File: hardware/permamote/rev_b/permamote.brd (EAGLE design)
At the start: 27 x 60 mm, 125 parts, among them J1 TC2030-JLINK-NL, J5 MICRO_USB_B_HIROSE_ZX62R-B-5P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, Q1 PMDXB950UPEL, Q10 PMDXB950UPEL, Q2 PMDXB950UPEL, Q3 PMDXB950UPEL, Q4 PMDXB950UPEL, Q5 PMDXB950UPEL, Q6 PMDXB950UPEL, Q7 PMDXB950UPEL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

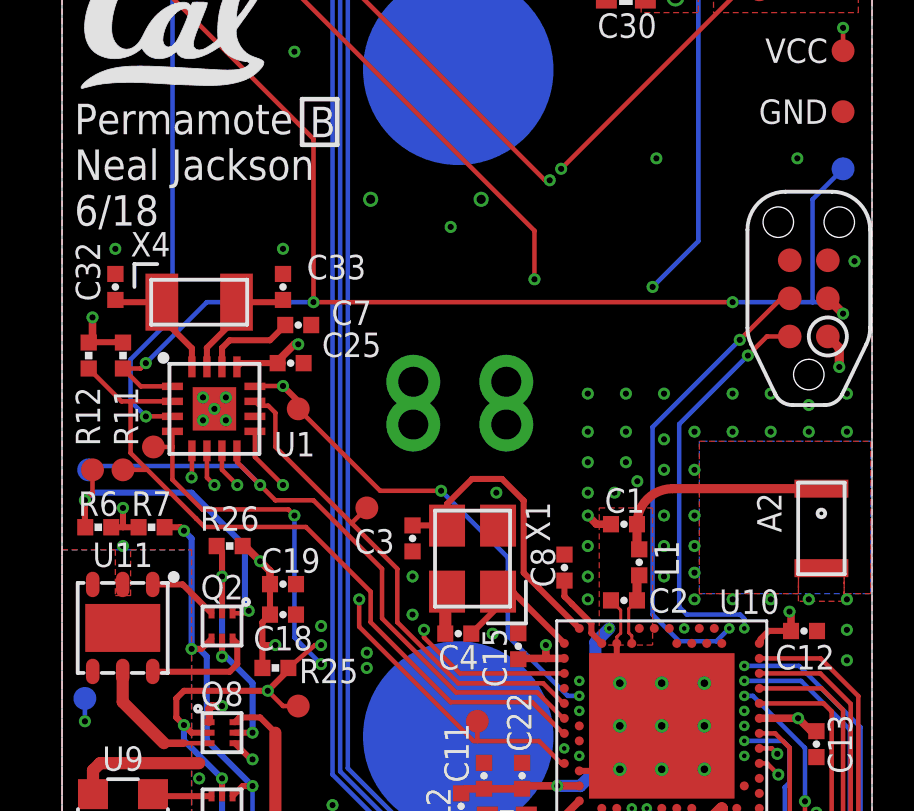
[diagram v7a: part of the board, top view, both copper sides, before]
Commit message: Update to nrf52840 v1.0 spec
Add decoupling cap to DEC5
Change values of RF passives
mentioned in #3
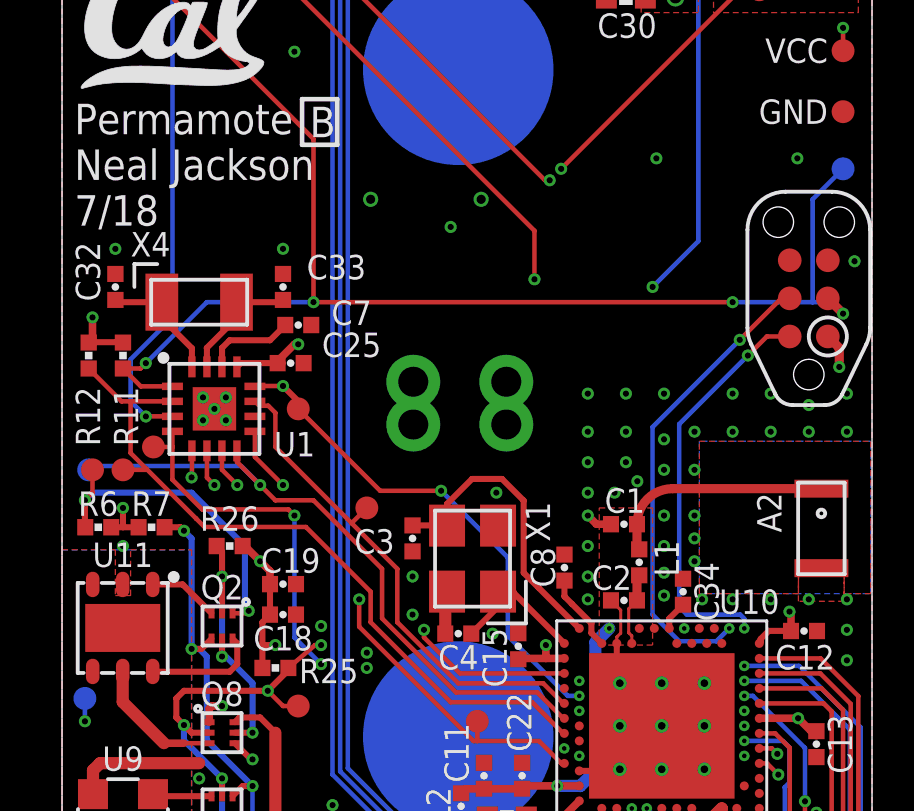
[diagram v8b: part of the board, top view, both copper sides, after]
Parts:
- added C34: 820pF, passives:0402_CAP
- C1: value 0.5pF -> 1pF
- C2: value 0.8pF -> 1pF
- L1: value 3.3nH -> 3.9nH
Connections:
- new net N$1: C34.1, U10.N24
- net GND: now also C34.2
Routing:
- net N$1: track 0.00 -> 0.98 mm
- net GND: vias 109 -> 110
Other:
- board text added: "Permamote Neal Jackson 7/18"
- board text removed: "Permamote Neal Jackson 6/18"
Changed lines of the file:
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@@
 <?xml version="1.0" encoding="utf-8"?>
 <!DOCTYPE eagle SYSTEM "eagle.dtd">
-<eagle version="9.0.0">
+<eagle version="9.0.1">
 <drawing>
 <settings>
@@
 <text x="0.413" y="37.349" size="1.016" layer="25" font="vector" ratio="12" align="top-left">Permamote
 Neal Jackson
-6/18</text>
+7/18</text>
 <polygon width="0.1016" layer="41">
 <vertex x="12.446" y="1.7907"/>
@@
 <attribute name="NAME" x="13.208" y="19.304" size="0.8128" layer="25" font="vector" ratio="12" rot="R180" align="bottom-center"/>
 </element>
-<element name="C2" library="passives" package="0402_CAP" value="0.8pF" x="18.732" y="20.793" smashed="yes" rot="R180">
-<attribute name="DIGIKEY" value="490-6269-1-ND" x="18.732" y="20.793" size="1.778" layer="27" rot="R180" display="off"/>
-<attribute name="MPN" value="GRM1555C1HR80BA01D " x="18.732" y="20.793" size="1.778" layer="27" rot="R180" display="off"/>
-<attribute name="NAME" x="20.228" y="20.383" size="0.8128" layer="25" font="vector" ratio="12" align="bottom-center"/>
-</element>
-<element name="C1" library="passives" package="0402_CAP" value="0.5pF" x="18.732" y="23.333" smashed="yes" rot="R180">
-<attribute name="DIGIKEY" value="490-6264-1-ND" x="18.732" y="23.333" size="1.778" layer="27" rot="R180" display="off"/>
-<attribute name="MPN" value="GRM1555C1HR50WA01D " x="18.732" y="23.333" size="1.778" layer="27" rot="R180" display="off"/>
+<element name="C2" library="passives" package="0402_CAP" value="1pF" x="18.732" y="20.793" smashed="yes" rot="R180">
+<attribute name="DIGIKEY" value="1276-1595-1-ND" x="18.732" y="20.793" size="1.778" layer="27" rot="R180" display="off"/>
+<attribute name="MPN" value="CL05C010CB5NNNC" x="18.732" y="20.793" size="1.778" layer="27" rot="R180" display="off"/>
+<attribute name="NAME" x="18.323" y="21.145" size="0.8128" layer="25" font="vector" ratio="12" align="bottom-center"/>
+</element>
+<element name="C1" library="passives" package="0402_CAP" value="1pF" x="18.732" y="23.333" smashed="yes" rot="R180">
+<attribute name="DIGIKEY" value="1276-1595-1-ND" x="18.732" y="23.333" size="1.778" layer="27" rot="R180" display="off"/>
+<attribute name="MPN" value="CL05C010CB5NNNC" x="18.732" y="23.333" size="1.778" layer="27" rot="R180" display="off"/>
 <attribute name="NAME" x="18.7574" y="23.714" size="0.8128" layer="25" font="vector" ratio="12" align="bottom-center"/>
 </element>
-<element name="L1" library="passives" package="0402_CAP" value="3.3nH" x="19.24" y="22.063" smashed="yes" rot="R270">
-<attribute name="DIGIKEY" value="535-10426-1-ND" x="19.24" y="22.063" size="1.778" layer="27" rot="R270" display="off"/>
-<attribute name="MPN" value="AISC-0402-3N3J-T " x="19.24" y="22.063" size="1.778" layer="27" rot="R270" display="off"/>
+<element name="L1" library="passives" package="0402_CAP" value="3.9nH" x="19.24" y="22.063" smashed="yes" rot="R270">
+<attribute name="DIGIKEY" value="490-1131-1-ND" x="19.24" y="22.063" size="1.778" layer="27" rot="R270" display="off"/>
+<attribute name="MPN" value="LQP15MN3N9B02D" x="19.24" y="22.063" size="1.778" layer="27" rot="R270" display="off"/>
 <attribute name="NAME" x="19.748" y="22.19" size="0.8128" layer="25" font="vector" ratio="12" rot="R270" align="bottom-center"/>
 </element>
@@
 <attribute name="MPN" value="TCS34725FN" x="25.146" y="2.159" size="1.778" layer="27" display="off"/>
 <attribute name="NAME" x="26.654" y="4.315" size="0.8128" layer="23" font="vector" ratio="12" rot="R180"/>
+</element>
+<element name="C34" library="passives" package="0402_CAP" value="820pF" x="20.701" y="21.082" smashed="yes" rot="R90">
+<attribute name="DIGIKEY" value="1276-6535-1-ND" x="20.701" y="21.082" size="1.778" layer="27" rot="R90" display="off"/>
+<attribute name="MPN" value="CL05B821KO5NNNC" x="20.701" y="21.082" size="1.778" layer="27" rot="R90" display="off"/>
+<attribute name="NAME" x="21.082" y="21.082" size="0.8128" layer="25" font="vector" ratio="12" rot="R270" align="bottom-center"/>
 </element>
 </elements>
@@
 <via x="17.526" y="23.622" extent="1-16" drill="0.2032"/>
 <via x="17.526" y="24.384" extent="1-16" drill="0.2032"/>
-<via x="21.082" y="22.606" extent="1-16" drill="0.2032"/>
-<via x="21.082" y="21.717" extent="1-16" drill="0.2032"/>
-<via x="21.082" y="20.828" extent="1-16" drill="0.2032"/>
+<via x="21.082" y="22.86" extent="1-16" drill="0.2032"/>
+<via x="20.066" y="21.717" extent="1-16" drill="0.2032"/>
+<via x="20.066" y="20.955" extent="1-16" drill="0.2032"/>
 <via x="22.352" y="20.828" extent="1-16" drill="0.2032"/>
 <via x="23.622" y="20.828" extent="1-16" drill="0.2032"/>
@@
 <via x="20.066" y="23.622" extent="1-16" drill="0.2032"/>
 <via x="20.066" y="22.606" extent="1-16" drill="0.2032"/>
-<via x="20.066" y="21.59" extent="1-16" drill="0.2032"/>
 <contactref element="D1" pad="-"/>
 <contactref element="TP27" pad="P$1"/>
@@
 <via x="24.511" y="35.528" extent="1-16" drill="0.2032"/>
 <via x="26.416" y="32.099" extent="1-16" drill="0.2032"/>
+<contactref element="C34" pad="2"/>
+<via x="21.336" y="20.828" extent="1-16" drill="0.2032"/>
+<via x="21.082" y="22.098" extent="1-16" drill="0.2032"/>
 </signal>
 <signal name="N$8">
@@
 <wire x1="20.574" y1="20.026" x2="20.574" y2="28.956" width="0.1524" layer="2"/>
 </signal>
+<signal name="N$1">
+<contactref element="U10" pad="N24"/>
+<contactref element="C34" pad="1"/>
+<wire x1="20.242" y1="19.86" x2="20.242" y2="20.18993125" width="0.2032" layer="1"/>
+<wire x1="20.242" y1="20.18993125" x2="20.701" y2="20.64893125" width="0.2032" layer="1"/>
+</signal>
 </signals>
